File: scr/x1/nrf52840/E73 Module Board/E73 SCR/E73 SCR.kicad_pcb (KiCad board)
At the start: 2 copper layers, 39.4 x 29.7 mm, 29 parts, among them J1 USB_B_Micro, J2 BAT, J3 SWD, J4 EXP, J5 SWTCH, J6 JOY, Q1 AO3401, U1 AP2112K-3.3, U2 MCP73831-2-OT, U3 E73-2G4M08S1C-52840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

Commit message: PCB v1.0
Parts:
- removed J4: EXP, Connectors_JST:JST_PH_B6B-PH-K_06x2.00mm_Straight
- added RST1: SW_SPST, Switches:Tac_SPST_RightAngle_SideActuated_THT, F.Cu at (129.5, 64.2)
- added SW1: SW_BAT, Switches:OS102011MA1QN1, F.Cu at (144.1, 64.2)
- C3, C5, D1, Q1, R1, R2: moved to B.Cu
- moved J2 20.9 mm to (149.8, 70.6), turned to 90 degrees
- moved D1 12.9 mm to (140.1, 77.7), turned to 0 degrees
- moved D3 12.9 mm to (137.2, 60.1)
- moved C6 12.0 mm to (145.0, 79.4), turned to 270 degrees
- moved Q1 10.6 mm to (131.7, 73.2), turned to 180 degrees
- moved RPROG1 9.93 mm to (146.0, 74.1), turned to 0 degrees
- moved J1 9.73 mm to (113.8, 64.4), turned to 270 degrees
- moved R4 9.59 mm to (137.2, 62.0)
- moved C5 7.65 mm to (131.2, 68.8), turned to 0 degrees
- moved J3 6.60 mm to (121.7, 67.5), turned to 180 degrees
- moved R1 5.93 mm to (135.7, 65.5)
- moved J6 5.33 mm to (130.2, 87.0), turned to 180 degrees
- moved C1 4.49 mm to (136.2, 73.5), turned to 90 degrees
- moved C8 4.04 mm to (140.6, 81.9)
- moved Y1 4.04 mm to (135.3, 84.5)
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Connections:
- J3 pad 1: SWDIO -> +3V3
- J3 pad 10: GND -> RESET
- J3 pad 2: +3V3 -> SWDIO
- J3 pad 3: SWCLK -> GND
- J3 pad 4: GND -> SWCLK
- J3 pad 5: Net-(J3-Pad5) -> GND
- J3 pad 6: GND -> Net-(J3-Pad6)
- J3 pad 8: GND -> Net-(J3-Pad8)
- J3 pad 9: RESET -> GND
- U1 pad 3: Net-(R2-Pad2) -> Net-(SW1-Pad2)
- U3 pad 33: P1_13 -> Net-(U3-Pad33)
- U3 pad 35: P0_24 -> Net-(U3-Pad35)
- U3 pad 41: P0_09 -> Net-(U3-Pad41)
- U3 pad 43: P0_10 -> Net-(U3-Pad43)
- U3 pad 8: X -> Y
- U3 pad 9: Y -> X
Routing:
- net +3V3: track 67.7 -> 109.4 mm, vias 1 -> 2
- net VBUS: track 30.6 -> 61.2 mm
- net LCLK: track 0.00 -> 27.5 mm
- net A1_P003: track 30.3 -> 4.82 mm, vias 1 -> 0
- net SW: track 24.6 -> 4.66 mm, vias 1 -> 0
- net Y: track 18.6 -> 4.47 mm
- net X: track 18.0 -> 4.14 mm
- net GND: track 53.6 -> 66.6 mm, vias 3 -> 10
- net Net-(SW1-Pad2): track 0.00 -> 8.81 mm
- net +BATT: track 30.1 -> 38.0 mm, vias 1 -> 2
- net Net-(RPROG1-Pad1): track 1.70 -> 9.46 mm
- net Net-(C3-Pad1): track 23.0 -> 30.6 mm, vias 0 -> 2
- net D-: track 5.02 -> 12.6 mm
- net SWDIO: track 11.0 -> 3.58 mm, vias 0 -> 1
- net D+: track 4.77 -> 11.1 mm
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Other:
- board size 39.4 x 29.7 mm -> 40 x 32 mm
- net class VBUS added: clearance 0.25, trace_width 0.3, via_dia 0.8, via_drill 0.4
- board text added: "CRAP v1.0"
- board text added: "CRAP v1.0 2019-04 For Shane Thomson By Ben Von Handorf"

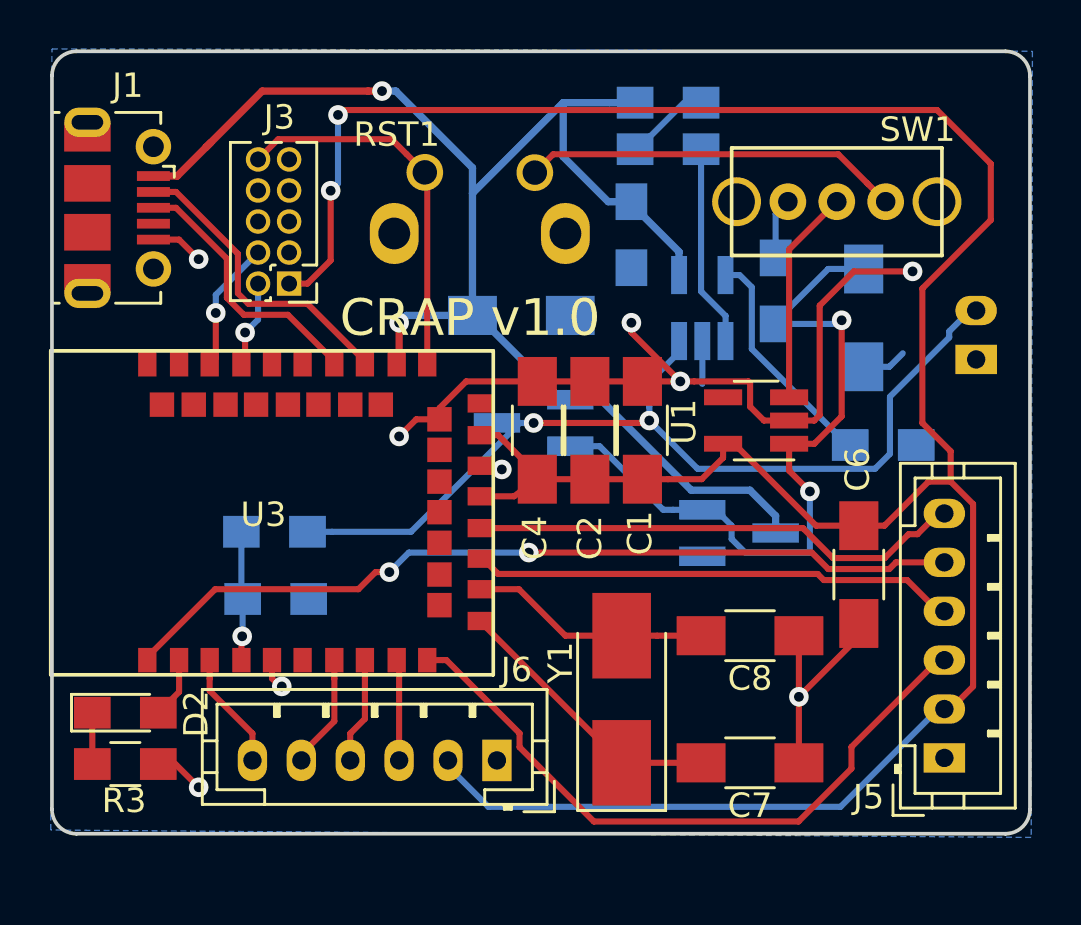
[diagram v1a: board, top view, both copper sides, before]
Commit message: WIP on E73 board bring up.  Requires new variant of board file not using LCXO
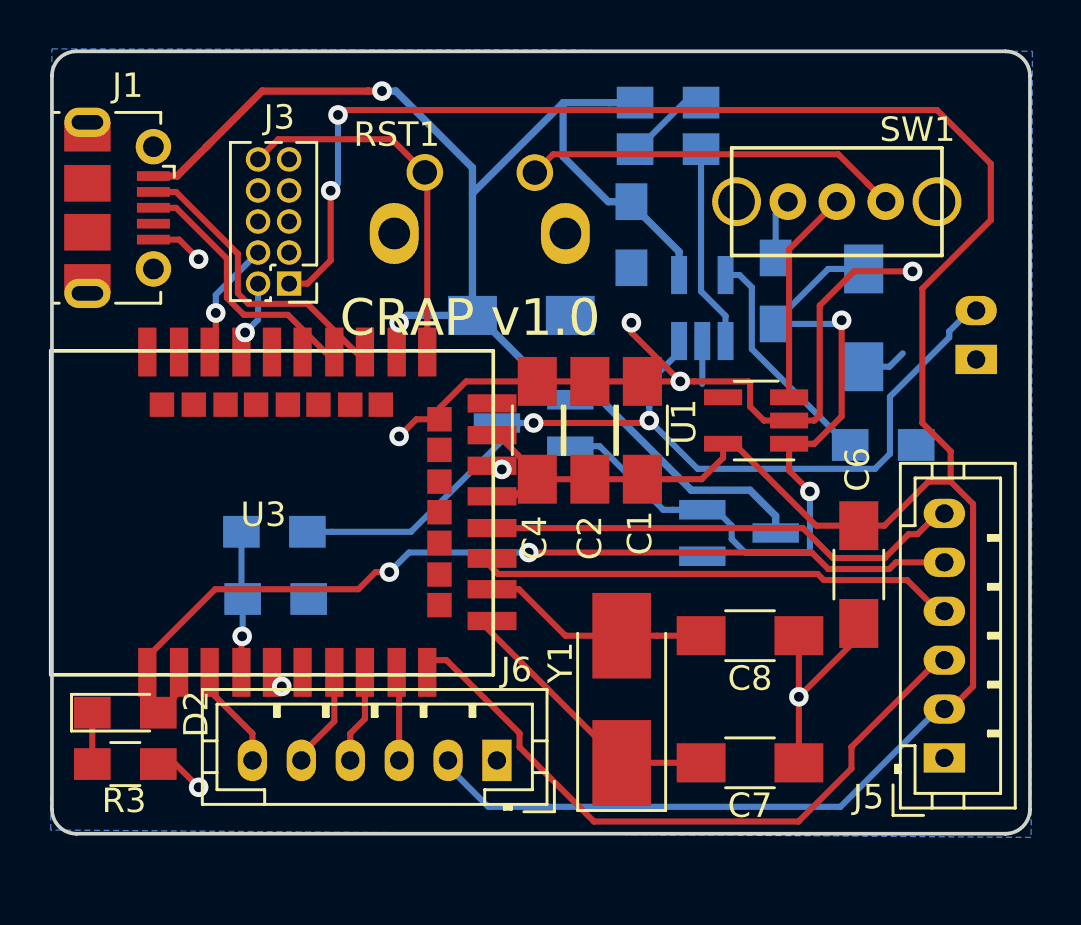
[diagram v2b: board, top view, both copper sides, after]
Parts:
- U3: footprint nrf52:E73(2G4M08S1C) -> nrf52:E73(2G4M08S1C)-HandSoldered
